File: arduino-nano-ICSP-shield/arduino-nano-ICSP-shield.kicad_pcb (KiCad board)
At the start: 2 copper layers, 43.2 x 17.8 mm, 14 parts, among them J1 Analog, J2 Digital, J3 AVR-ISP-6

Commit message: continue
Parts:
- removed R2, R3: R, Resistor_SMD:R_0805_2012Metric_Pad1.20x1.40mm_HandSolder
- C1: footprint Capacitor_SMD:C_0805_2012Metric_Pad1.18x1.45mm_HandSolder -> Capacitor_SMD:C_0603_1608Metric; moved to F.Cu
- D1, D2, D3: footprint LED_SMD:LED_0805_2012Metric_Pad1.15x1.40mm_HandSolder -> LED_SMD:LED_0603_1608Metric
- R1: value R -> 140Ω; footprint Resistor_SMD:R_0805_2012Metric_Pad1.20x1.40mm_HandSolder -> Resistor_SMD:R_0603_1608Metric; moved to F.Cu
- moved R1 32.7 mm to (141.0, 88.5), turned to 0 degrees
- moved C1 26.1 mm to (141.0, 94.0), turned to 0 degrees
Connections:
- D1 pad 1: GND -> Net-(D1-K)
- D1 pad 2: Net-(D1-A) -> heartbeat
- D2 pad 1: GND -> Net-(D1-K)
- D2 pad 2: Net-(D2-A) -> error
- D3 pad 1: GND -> Net-(D1-K)
- D3 pad 2: Net-(D3-A) -> programming
- R1 pad 1: heartbeat -> Net-(D1-K)
- R1 pad 2: Net-(D1-A) -> GND
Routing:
- net /~{RESET}: track 36.7 -> 0.00 mm
- net sck: track 33.9 -> 0.00 mm
- net miso: track 32.3 -> 0.00 mm
- net mosi: track 29.2 -> 0.00 mm, vias 1 -> 0
- net reset: track 22.9 -> 0.00 mm, vias 1 -> 0
- net programming: track 14.5 -> 0.00 mm
- net error: track 9.92 -> 0.00 mm
- net VCC: track 9.28 -> 0.00 mm
- net heartbeat: track 5.37 -> 0.00 mm
- net Net-(D1-A): track 3.28 -> 0.00 mm, vias 1 -> 0
- net Net-(D2-A): track 3.26 -> 0.00 mm, vias 1 -> 0
- net Net-(D3-A): track 3.18 -> 0.00 mm, vias 1 -> 0

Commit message: move parts to the back
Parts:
- C1, R1: moved to B.Cu
- moved C1 28.4 mm to (112.6, 93.6), turned to 180 degrees
- moved R1 28.4 mm to (112.6, 88.6), turned to 180 degrees

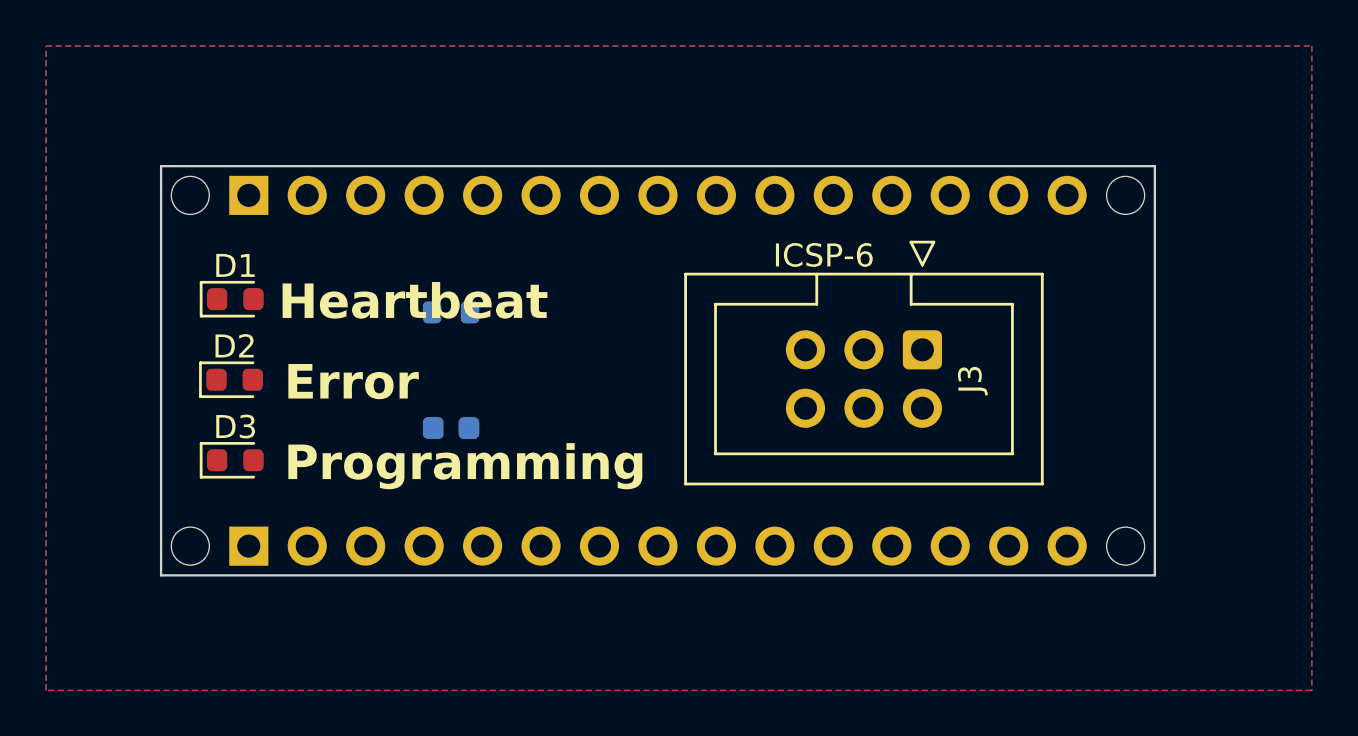
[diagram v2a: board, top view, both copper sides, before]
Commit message: remove linked pins & route
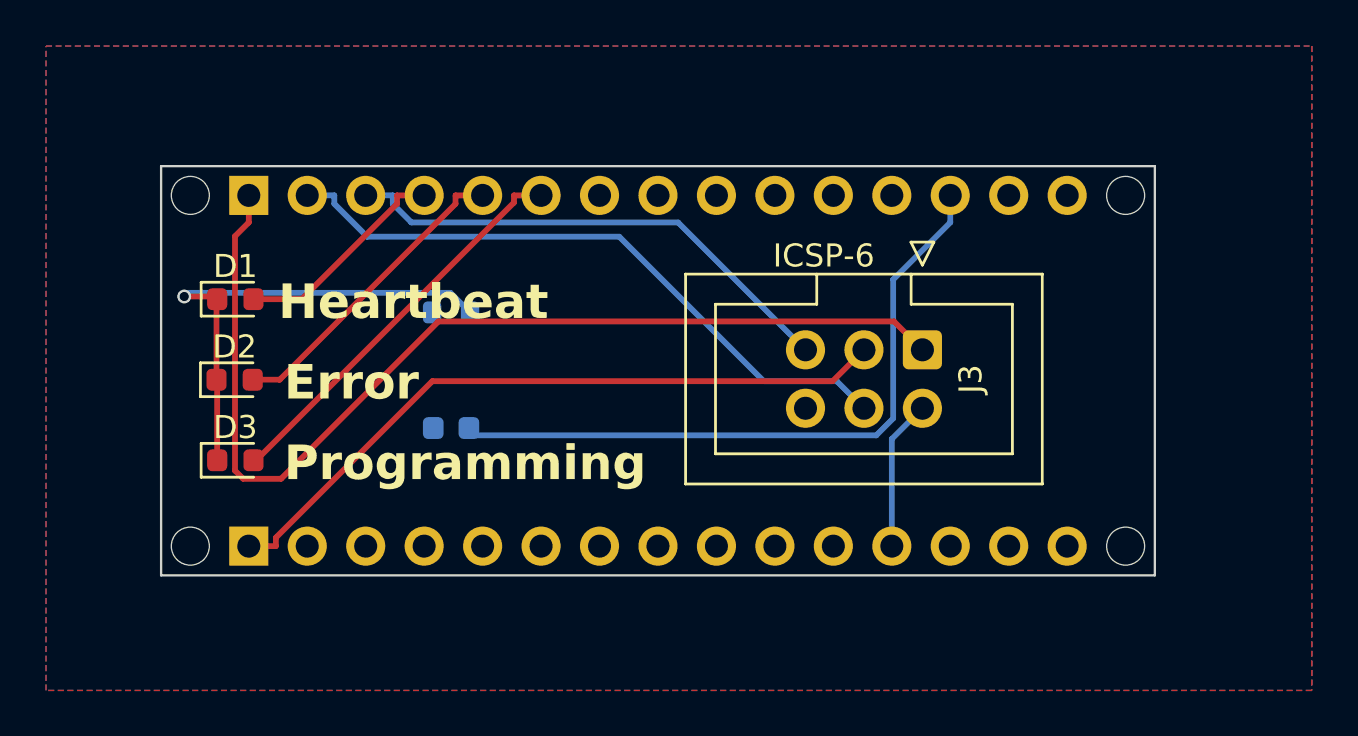
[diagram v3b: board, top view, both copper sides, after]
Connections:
- J1 pad 13: /~{RESET} -> /~{RESET2}
- J1 pad 14: GND -> GND2
- J3 pad 2: VCC -> +5V
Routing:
- net miso: track 0.00 -> 45.6 mm
- net sck: track 0.00 -> 30.5 mm
- net /~{RESET}: track 0.00 -> 29.6 mm
- net mosi: track 0.00 -> 28.2 mm
- net reset: track 0.00 -> 22.1 mm
- net Net-(D1-K): track 0.00 -> 21.3 mm, vias 0 -> 1
- net programming: track 0.00 -> 17.4 mm
- net error: track 0.00 -> 13.5 mm
- net heartbeat: track 0.00 -> 9.50 mm
- net +5V: track 0.00 -> 6.54 mm

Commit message: flip resistor
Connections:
- R1 pad 1: Net-(D1-K) -> GND
- R1 pad 2: GND -> Net-(D1-K)
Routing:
- net Net-(D1-K): track 21.3 -> 19.6 mm
- net /~{RESET}: track 29.6 -> 30.4 mm
- net mosi: track 28.2 -> 28.8 mm

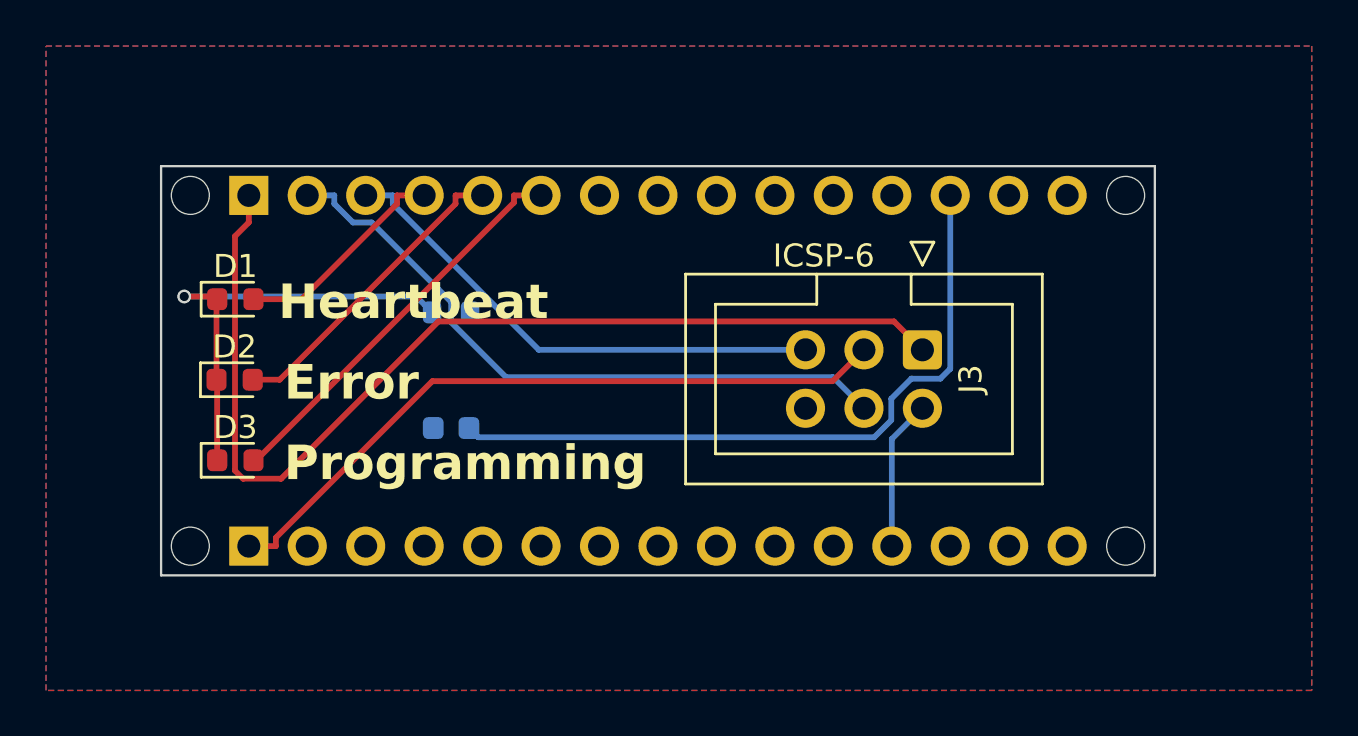
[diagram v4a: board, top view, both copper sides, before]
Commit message: routed by hand
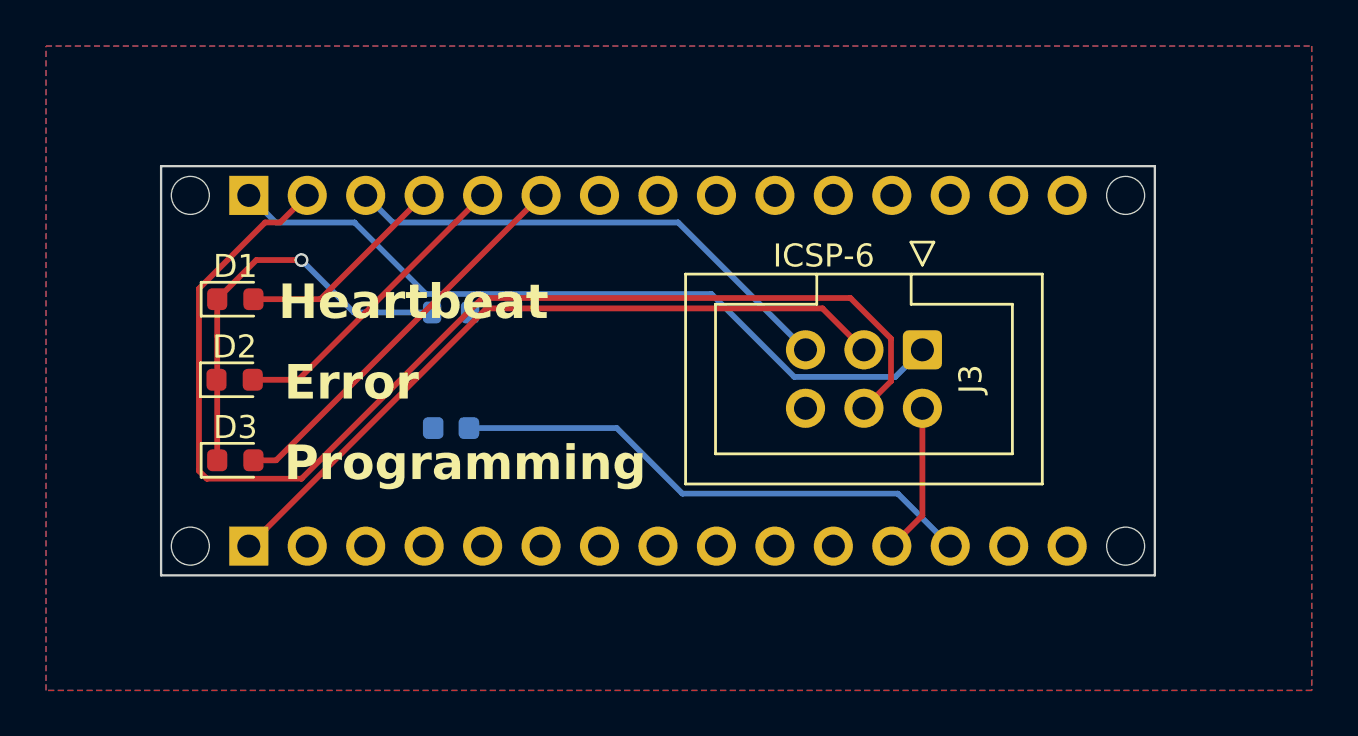
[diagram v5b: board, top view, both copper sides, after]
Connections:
- J1 pad 13: /~{RESET2} -> /~{RESET}
- J2 pad 13: /~{RESET} -> /~{RESET2}
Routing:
- net mosi: track 28.8 -> 52.0 mm
- net miso: track 45.6 -> 33.0 mm
- net /~{RESET}: track 30.4 -> 23.0 mm
- net Net-(D1-K): track 19.6 -> 18.0 mm
- net sck: track 30.5 -> 31.8 mm

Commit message: updated
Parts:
- added R2: 100Ω, Resistor_SMD:R_0603_1608Metric, B.Cu at (118.7, 90.5)
- added R3: 100Ω, Resistor_SMD:R_0603_1608Metric, B.Cu at (118.5, 94.0)
- R1: value 140Ω -> 100Ω
- moved C1 26.3 mm to (138.3, 87.8)
- moved R1 6.35 mm to (118.8, 87.0), turned to 0 degrees
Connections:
- D1 pad 1: Net-(D1-K) -> GND
- D1 pad 2: heartbeat -> Net-(D1-A)
- D2 pad 1: Net-(D1-K) -> GND
- D2 pad 2: error -> Net-(D2-A)
- D3 pad 1: Net-(D1-K) -> GND
- D3 pad 2: programming -> Net-(D3-A)
- J1 pad 14: GND2 -> GND
- J2 pad 13: /~{RESET2} -> /~{RESET}
- R1 pad 1: GND -> Net-(D1-A)
- R1 pad 2: Net-(D1-K) -> heartbeat
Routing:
- net Net-(D1-K): track 18.0 -> 0.00 mm, vias 1 -> 0
- net Net-(D3-A): track 0.00 -> 17.2 mm, vias 0 -> 1
- net Net-(D2-A): track 0.00 -> 17.2 mm, vias 0 -> 1
- net mosi: track 52.0 -> 35.6 mm
- net Net-(D1-A): track 0.00 -> 14.6 mm, vias 0 -> 1
- net miso: track 33.0 -> 38.4 mm
- net programming: track 17.3 -> 13.2 mm
- net /~{RESET}: track 23.0 -> 20.0 mm
- net error: track 13.3 -> 10.4 mm, vias 0 -> 1
- net sck: track 31.8 -> 33.9 mm
- net heartbeat: track 9.29 -> 9.97 mm
- net reset: track 21.9 -> 22.1 mm, vias 0 -> 1

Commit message: Readd Clip
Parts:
- added J4: Conn_02x04_Counter_Clockwise, CustomLibrary:PinHeader_2x04_P2.54mm_Vertical_Counterclockwise-Clip, F.Cu at (118.3, 87.9)
- moved C1 4.37 mm to (140.8, 91.3), turned to 90 degrees
- moved R1 4.33 mm to (114.4, 87.2)
- moved R3 4.33 mm to (114.2, 94.2)
- moved R2 4.33 mm to (114.4, 90.8)
- moved J3 2.33 mm to (135.4, 90.4)
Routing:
- net +5V: track 6.54 -> 21.8 mm
- net Net-(D3-A): track 17.2 -> 10.2 mm
- net Net-(D2-A): track 17.2 -> 11.6 mm
- net Net-(D1-A): track 14.6 -> 9.90 mm
- net heartbeat: track 9.97 -> 6.03 mm
- net reset: track 22.1 -> 24.7 mm, vias 1 -> 0
- net error: track 10.4 -> 8.45 mm, vias 1 -> 0
- net programming: track 13.2 -> 11.4 mm
- net /~{RESET}: track 20.0 -> 21.5 mm
- net miso: track 38.4 -> 39.8 mm, vias 0 -> 1
- net mosi: track 35.6 -> 36.7 mm
- net GND: vias 0 -> 1

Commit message: improv
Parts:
- removed J4: Conn_02x04_Counter_Clockwise, CustomLibrary:PinHeader_2x04_P2.54mm_Vertical_Counterclockwise-Clip
- C1, R1, R2, R3: moved to F.Cu
- moved C1 23.4 mm to (117.3, 91.5), turned to 180 degrees
- moved R2 7.39 mm to (107.0, 91.5)
- moved R3 7.39 mm to (106.8, 95.0)
- moved R1 7.36 mm to (107.1, 88.0)
- moved J3 3.56 mm to (131.8, 90.4)
- moved D1 0.24 mm to (103.5, 88.0)
- moved D2 0.24 mm to (103.4, 91.5)
- moved D3 0.24 mm to (103.5, 95.0)
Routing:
- net +5V: track 21.8 -> 5.87 mm
- net /~{RESET}: track 21.5 -> 35.0 mm
- net mosi: track 36.7 -> 27.1 mm
- net Net-(D2-A): track 11.6 -> 1.97 mm, vias 1 -> 0
- net Net-(D3-A): track 10.2 -> 1.78 mm, vias 1 -> 0
- net Net-(D1-A): track 9.90 -> 2.03 mm, vias 1 -> 0
- net sck: track 33.9 -> 29.2 mm
- net miso: track 39.8 -> 35.2 mm, vias 1 -> 0
- net programming: track 11.4 -> 15.2 mm
- net reset: track 24.7 -> 20.9 mm
- net error: track 8.45 -> 10.5 mm
